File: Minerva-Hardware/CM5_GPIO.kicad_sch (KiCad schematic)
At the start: 15 parts, among them J14 JST_SHBM04B-SRSS-TB, J2 Conn_02x07_Odd_Even, J3 Conn_01x03, J8 THD-20-R, SW1 Right angle Tact button

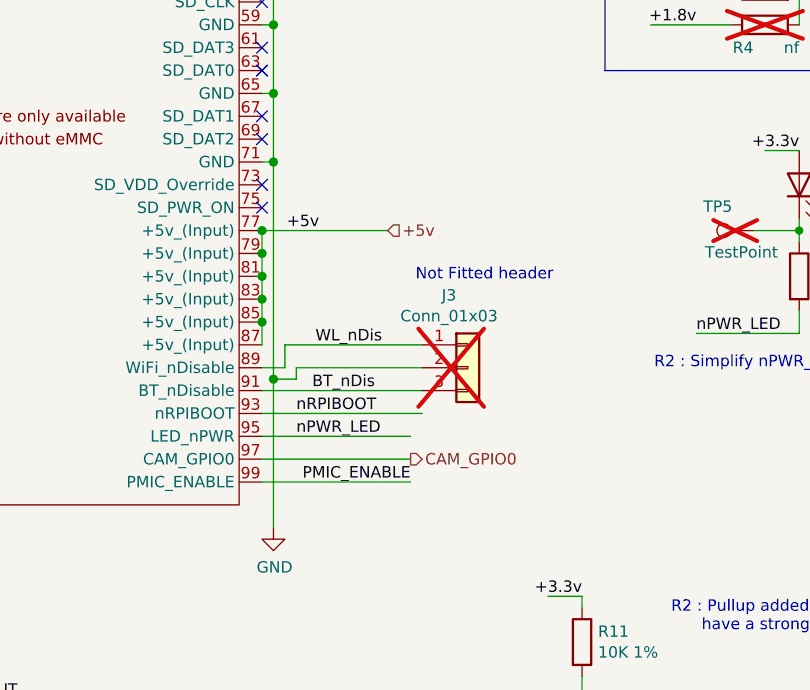
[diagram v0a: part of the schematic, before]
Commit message: Rename and commit actions due to mishap of location naming/saving
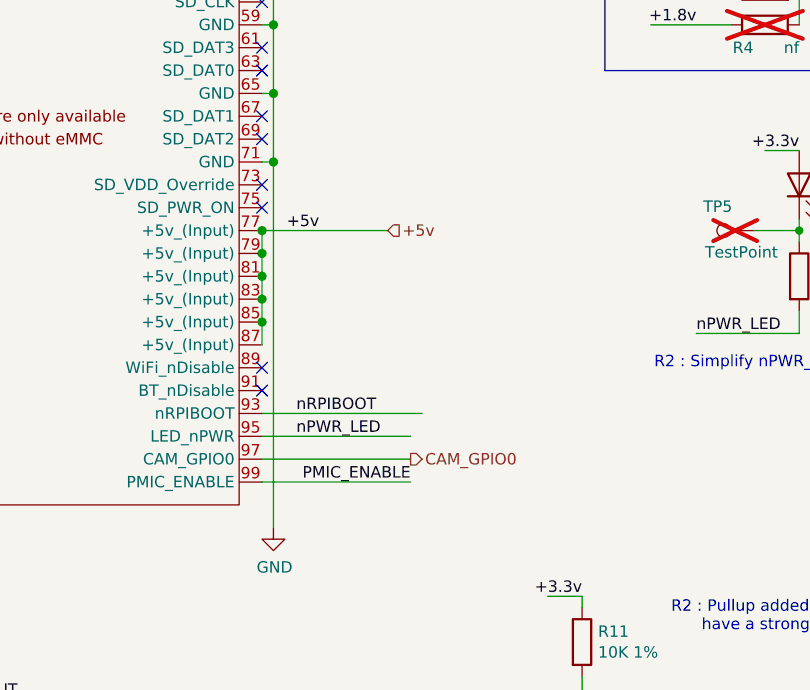
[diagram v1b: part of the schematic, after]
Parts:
- removed J3: Conn_01x03, Connector_PinHeader_2.54mm:PinHeader_1x03_P2.54mm_Vertical, symbol Connector_Generic:Conn_01x03
- J8: footprint Connector_PinHeader_2.54mm:PinHeader_2x20_P2.54mm_Vertical -> Connector_PinSocket_2.54mm:PinSocket_2x20_P2.54mm_Horizontal
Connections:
- net BT_nDis: no longer names the net of Module1.91 (BT_nDisable)
- net WL_nDis: no longer names the net of Module1.89 (WiFi_nDisable)
- no-connect marks 24 -> 26
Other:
- note removed: "Not Fitted header"

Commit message: renames
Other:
- company: Copyright © 2024 Raspberry Pi Ltd. -> (none)
- title: Compute Module 5 IO Board - GPIO - Ethernet -> Minerva Carrier Board - GPIO & LEDs
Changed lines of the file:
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@@
 	(paper "A4")
 	(title_block
-		(title "Compute Module 5 IO Board - GPIO - Ethernet")
+		(title "Minerva Carrier Board - GPIO & LEDs")
 		(rev "1")
-		(company "Copyright © 2024 Raspberry Pi Ltd.")
-		(comment 1 "www.raspberrypi.com")
 	)
 	(text "40Way GPIO Header"

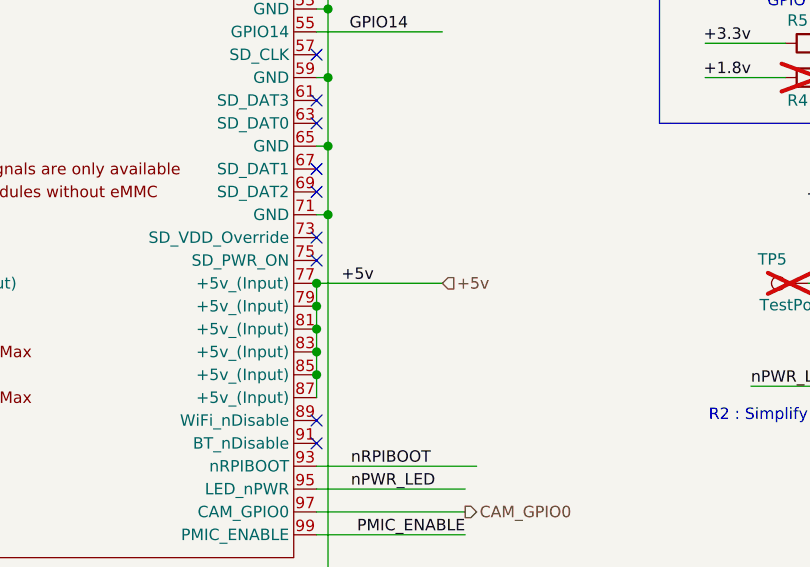
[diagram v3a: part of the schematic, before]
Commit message: Redid the BQ powerpath unit
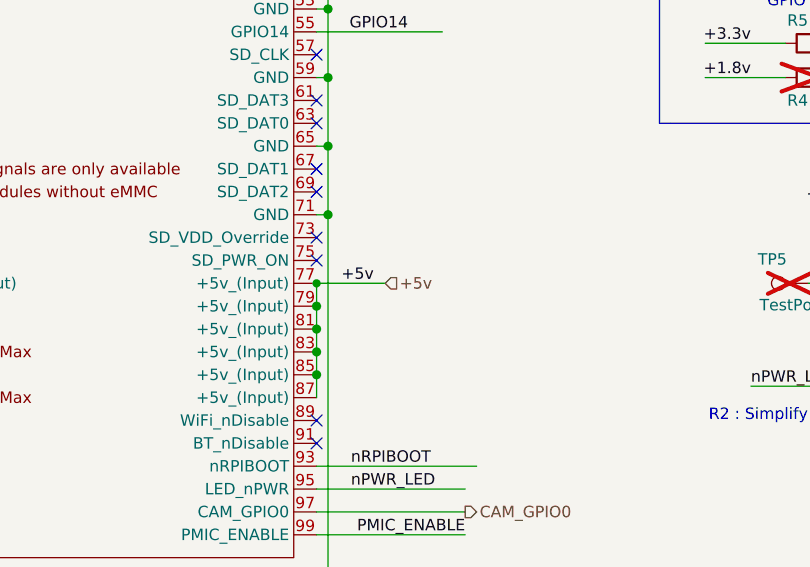
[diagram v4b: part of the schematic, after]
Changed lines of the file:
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@@
 	)
 	(junction
+		(at 100.33 118.11)
+		(diameter 0)
+		(color 0 0 0 0)
+	)
+	(junction
 		(at 101.6 36.83)
 		(diameter 1.016)
@@
 	)
 	(junction
-		(at 100.33 118.11)
-		(diameter 1.016)
-		(color 0 0 0 0)
-	)
-	(junction
 		(at 101.6 95.25)
 		(diameter 1.016)
@@
 	(wire
 		(pts
-			(xy 100.33 118.11) (xy 114.3 118.11)
-		)
-		(stroke
-			(width 0)
-			(type solid)
-		)
-	)
-	(wire
-		(pts
 			(xy 101.6 36.83) (xy 101.6 49.53)
 		)
@@
 	(wire
 		(pts
+			(xy 100.33 118.11) (xy 107.95 118.11)
+		)
+		(stroke
+			(width 0)
+			(type solid)
+		)
+	)
+	(wire
+		(pts
 			(xy 100.33 118.11) (xy 100.33 120.65)
 		)
@@
 	(hierarchical_label "+5v"
 		(shape input)
-		(at 114.3 118.11 0)
+		(at 107.95 118.11 0)
 		(effects
 			(font

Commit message: working on pcb more
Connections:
- net USBOTG: no longer names the net of J2.10 (Pin_10)
- no-connect marks 26 -> 27
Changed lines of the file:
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@@
+	)
+	(no_connect
+		(at 40.64 180.34)
 	)
 	(no_connect
@@
 	(wire
 		(pts
+			(xy 0.1588 2.2862) (xy 0.1588 11.1762)
+		)
+		(stroke
+			(width 0)
+			(type default)
+		)
+	)
+	(wire
+		(pts
 			(xy 140.97 57.15) (xy 152.4 57.15)
 		)
@@
 			(width 0)
 			(type solid)
-		)
-	)
-	(wire
-		(pts
-			(xy 40.64 180.34) (xy 54.61 180.34)
-		)
-		(stroke
-			(width 0)
-			(type default)
 		)
 	)
@@
 			)
 			(justify right bottom)
+		)
+	)
+	(label "+3.3v"
+		(at 0.1588 2.2862 0)
+		(effects
+			(font
+				(size 1.27 1.27)
+			)
+			(justify left bottom)
 		)
 	)
@@
 		(effects
 			(font
-				(size 1.27 1.27)
-			)
-			(justify left)
-		)
-	)
-	(hierarchical_label "USBOTG"
-		(shape output)
-		(at 54.61 180.34 0)
-		(effects
-			(font
